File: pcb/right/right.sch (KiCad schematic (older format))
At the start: 127 parts, among them J1 USB_B_Mini, J2 To Left Part, J3 ICSP, SW1 SW_Push, SW10 SW_Push, SW11 SW_Push, SW12 SW_Push, SW13 SW_Push, SW14 SW_Push, SW15 SW_Push, SW16 SW_Push, SW17 SW_Push, SW18 SW_Push, SW19 SW_Push, SW2 SW_Push, SW20 SW_Push, SW21 SW_Push, SW22 SW_Push, SW23 SW_Push, SW24 SW_Push, SW25 SW_Push, SW26 SW_Push, SW27 SW_Push, SW28 SW_Push, SW29 SW_Push, SW3 SW_Push, SW30 SW_Push, SW31 SW_Push, SW32 SW_Push, SW33 SW_Push, SW34 SW_Push, SW35 SW_Push, SW36 SW_Push, SW37 SW_Push, SW38 SW_Push, SW39 SW_Push, SW4 SW_Push, SW40 SW_Push, SW41 SW_Push, SW42 SW_Push, SW43 SW_Push, SW44 SW_Push, SW45 SW_Push, SW46 SW_Push, SW47 SW_Push, SW48 SW_Push, SW49 SW_Push, SW5 SW_Push, SW50 SW_Push, SW51 SW_Push, SW52 SW_Push, SW53 SW_Push, SW6 SW_Push, SW7 SW_Push, SW8 SW_Push, SW9 SW_Push, U1 ATmega32U4-AU, Y1 16MHz

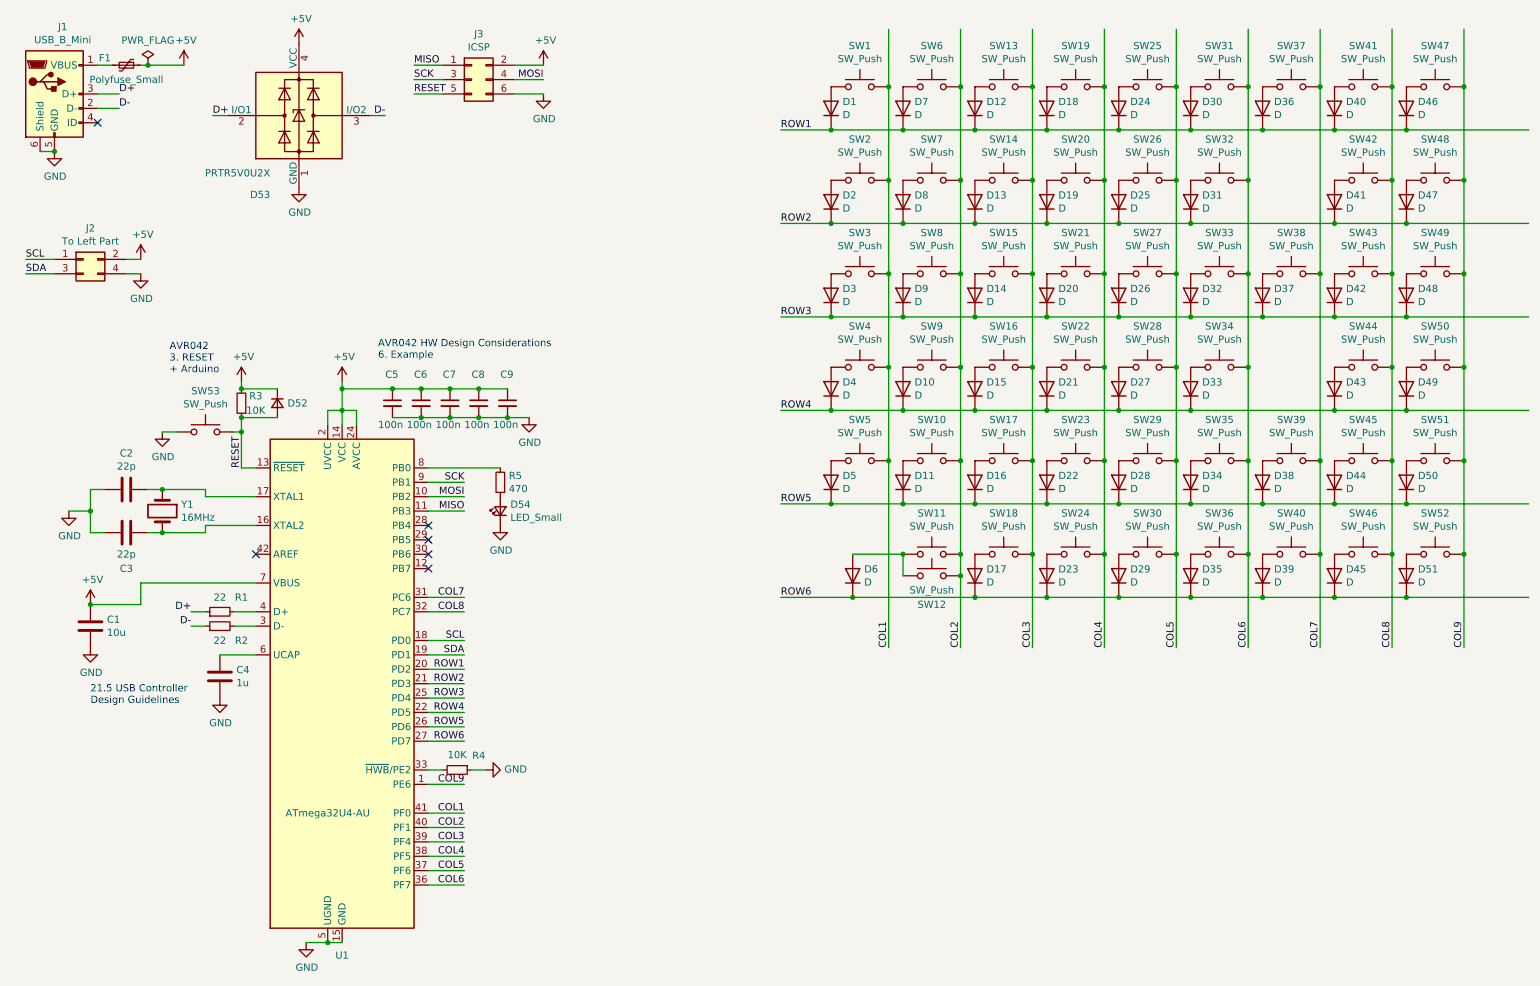
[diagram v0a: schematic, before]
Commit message: pcb: right: pullup for keys and i2c
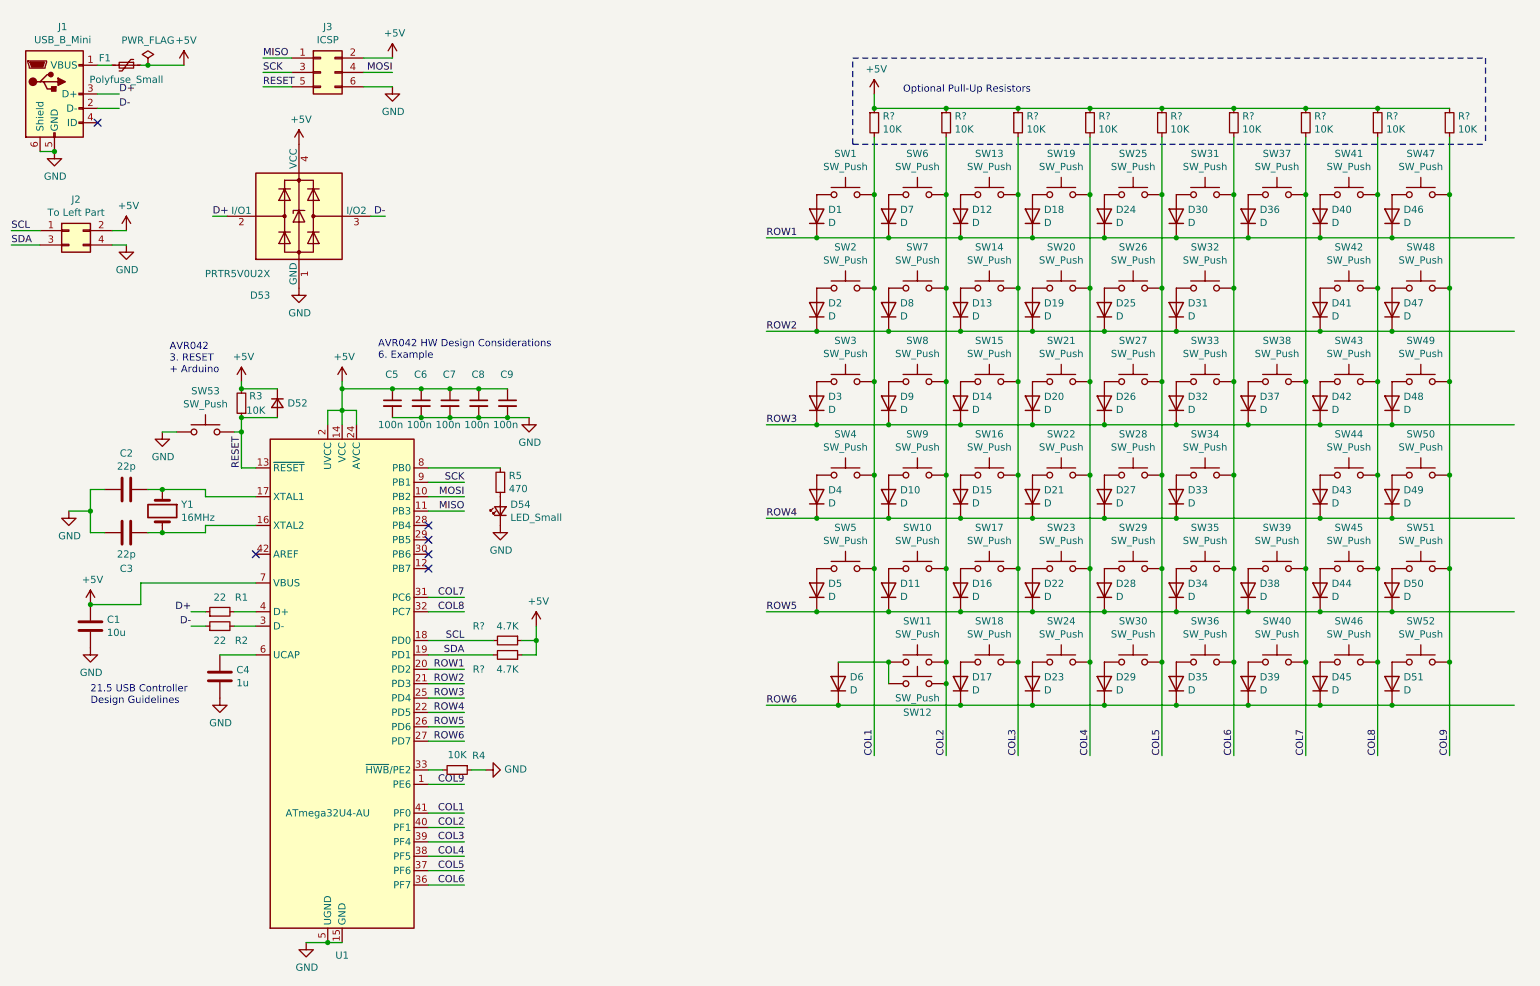
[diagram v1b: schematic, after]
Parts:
- added R? (x9): 10K, symbol Device:R_Small
- added R? (x2): 4.7K, symbol Device:R_Small
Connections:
- wire segments 209 -> 222
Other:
- note added: "Optional Pull-Up Resistors"
- moved on the sheet: D1, D10, D11, D12, D13, D14, D15, D16, D17, D18, D19, D2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

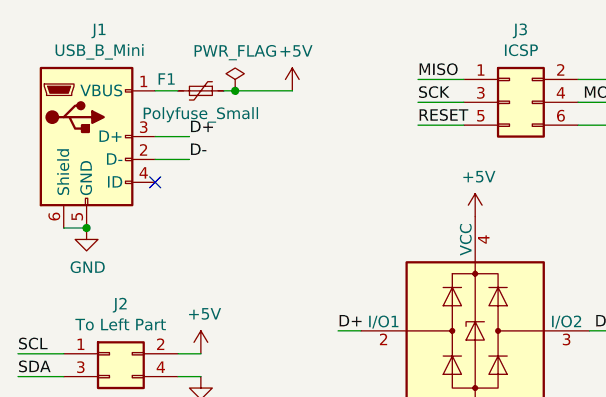
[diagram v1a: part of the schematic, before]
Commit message: pcb: right: fuse size
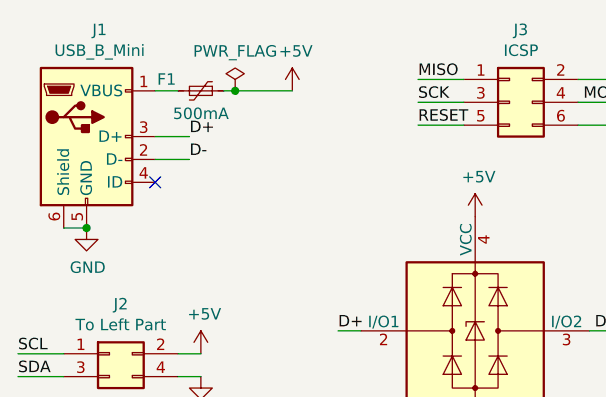
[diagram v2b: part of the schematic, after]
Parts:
- F1: value Polyfuse_Small -> 500mA
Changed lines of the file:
@@
 P 1350 900
 F 0 "F1" V 1300 750 50  0000 C CNN
-F 1 "Polyfuse_Small" V 1450 900 50  0000 C CNN
+F 1 "500mA" V 1450 900 50  0000 C CNN
 F 2 "" H 1400 700 50  0001 L CNN
 F 3 "~" H 1350 900 50  0001 C CNN
@@
 	0    1    -1   0
 $EndComp
-Wire Wire Line
-	3450 4900 3900 4900
-Wire Wire Line
-	3450 5000 3900 5000
 $Comp
 L power:+5V #PWR?
@@
 Wire Wire Line
 	4200 4900 4200 4800
+Wire Wire Line
+	3450 5000 3900 5000
+Wire Wire Line
+	3450 4900 3900 4900
 $EndSCHEMATC

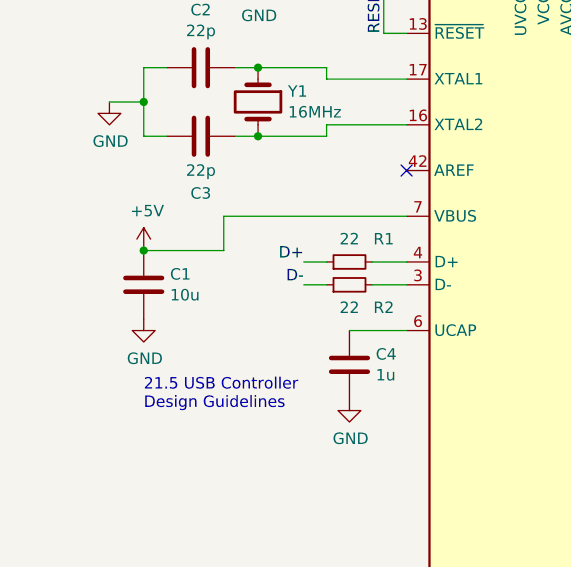
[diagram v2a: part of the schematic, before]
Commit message: pcb: right: Tanatalum capacitor
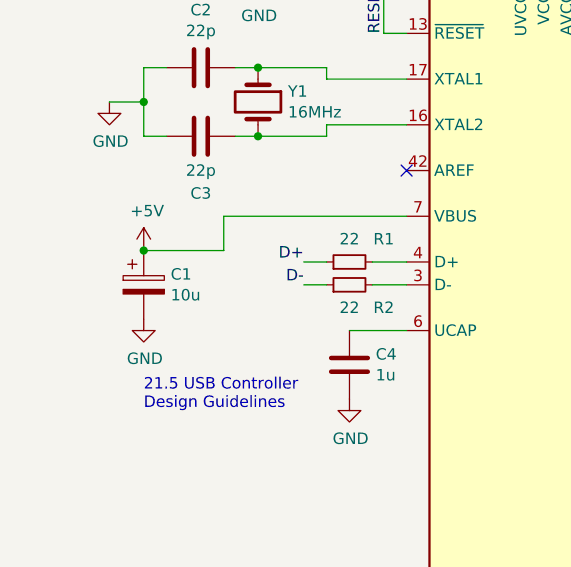
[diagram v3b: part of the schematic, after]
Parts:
- removed C1: 10u, symbol Device:C
- added C1: 10u, Capacitor_Tantalum_SMD:CP_EIA-3216-18_Kemet-A_Pad1.58x1.35mm_HandSolder, symbol Device:CP
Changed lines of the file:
@@
 	-1   0    0    1
 $EndComp
-$Comp
-L Device:C C1
-U 1 1 605E8000
-P 1100 4800
-F 0 "C1" H 1215 4846 50  0000 L CNN
-F 1 "10u" H 1215 4755 50  0000 L CNN
-F 2 "" H 1138 4650 50  0001 C CNN
-F 3 "~" H 1100 4800 50  0001 C CNN
-	1    1100 4800
-	1    0    0    -1
-$EndComp
 Wire Wire Line
 	2250 4500 1450 4500
@@
 Wire Wire Line
 	1450 4650 1100 4650
-Connection ~ 1100 4650
 $Comp
 L power:GND #PWR0111
@@
 Wire Wire Line
 	3450 4900 3900 4900
+$Comp
+L Device:CP C1
+U 1 1 6046FDA4
+P 1100 4800
+F 0 "C1" H 1218 4846 50  0000 L CNN
+F 1 "10u" H 1218 4755 50  0000 L CNN
+F 2 "Capacitor_Tantalum_SMD:CP_EIA-3216-18_Kemet-A_Pad1.58x1.35mm_HandSolder" H 1138 4650 50  0001 C CNN
+F 3 "~" H 1100 4800 50  0001 C CNN
+	1    1100 4800
+	1    0    0    -1
+$EndComp
+Connection ~ 1100 4650
 $EndSCHEMATC
